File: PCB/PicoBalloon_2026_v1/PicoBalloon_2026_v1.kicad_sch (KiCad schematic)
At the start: 3 parts, among them U1 ATmega328P-A, U2 RFM95W-868S2, U3 GP-02

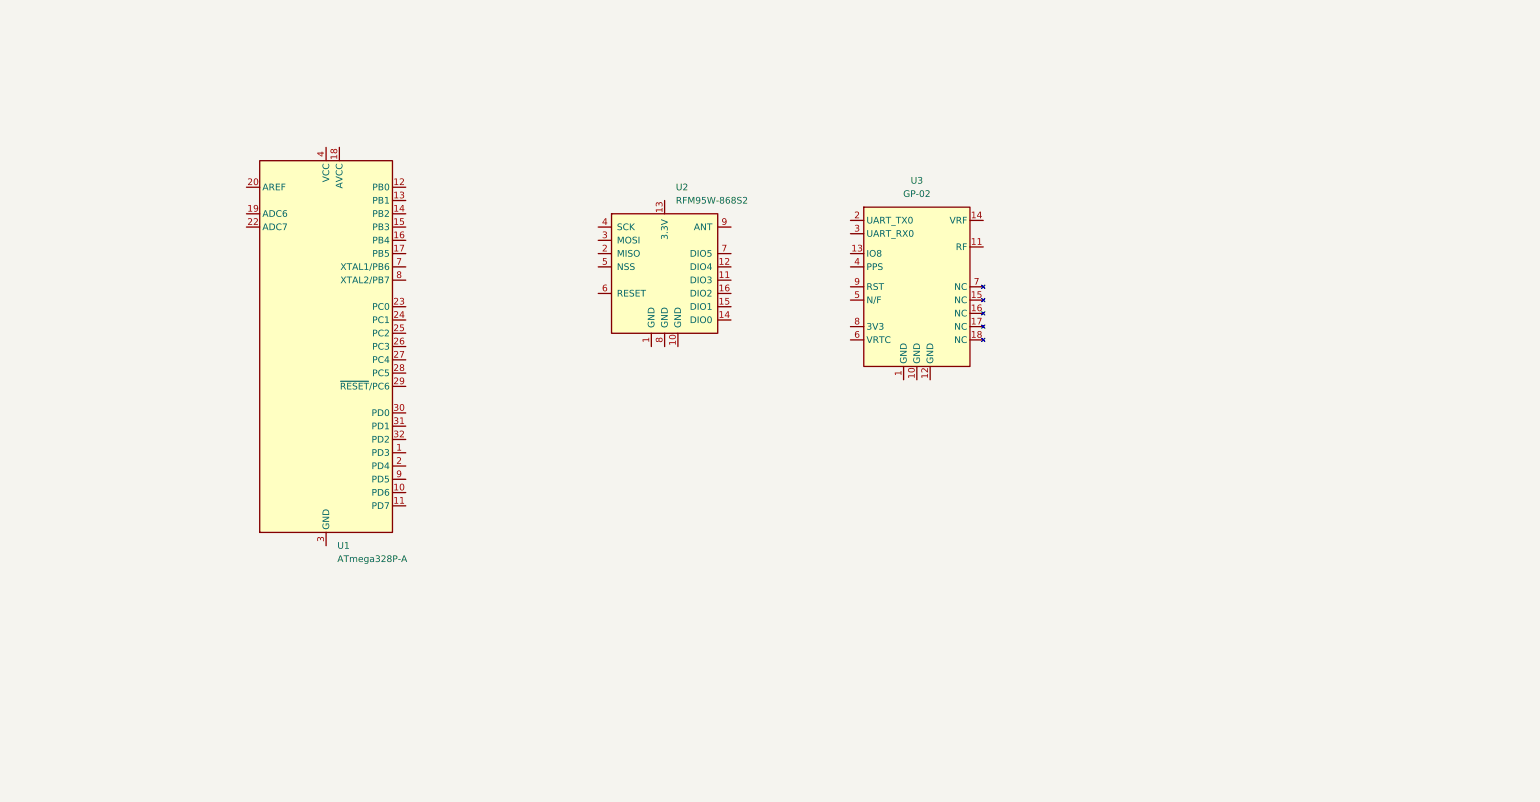
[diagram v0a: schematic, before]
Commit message: [PCB] Schematic update. LoRa power on, GPS power on, VBAT meas. power on.
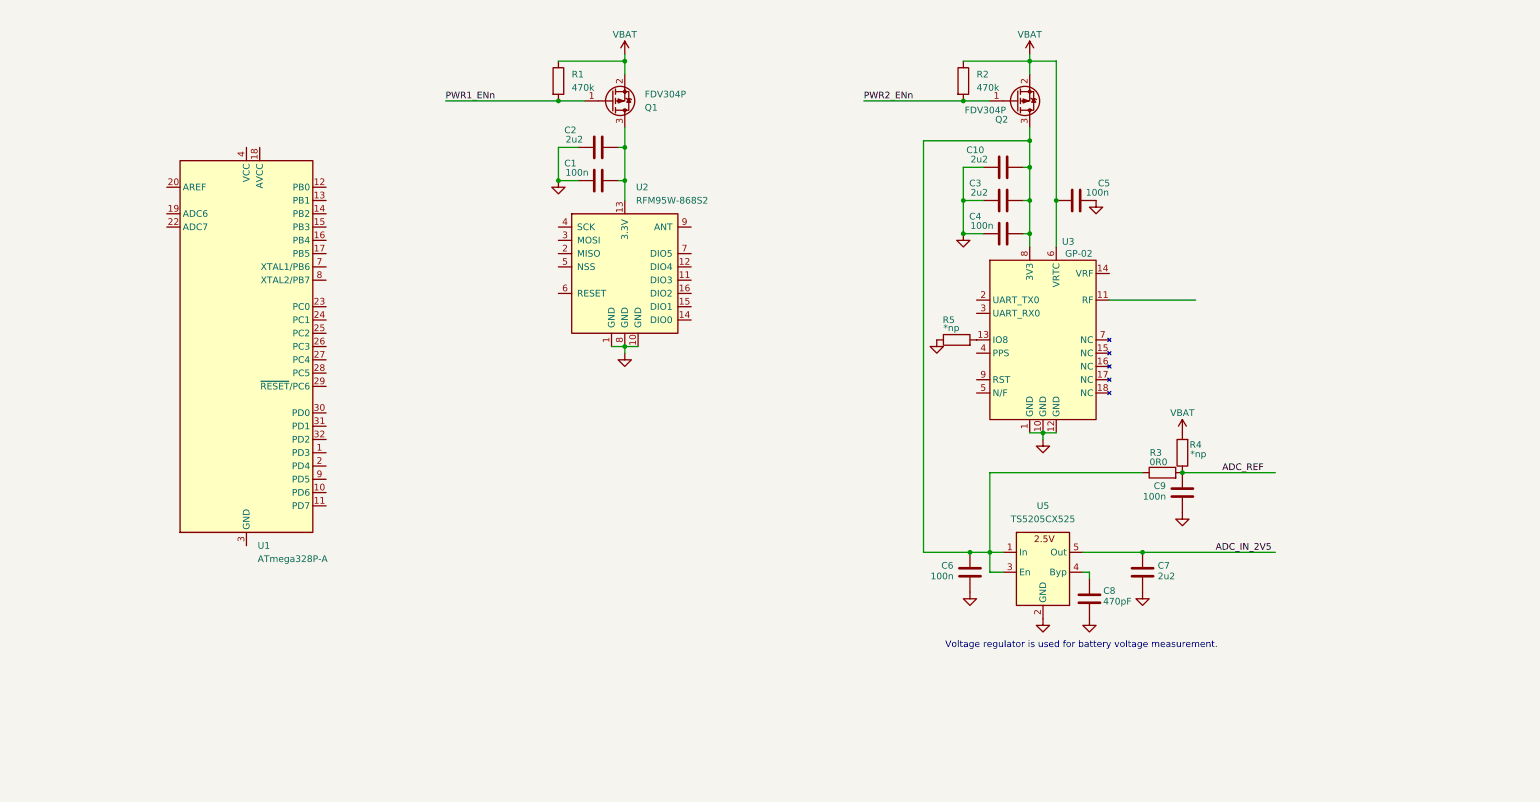
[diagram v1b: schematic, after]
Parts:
- added C1, C4, C5, C6, C9: 100n, Capacitor_SMD:C_0805_2012Metric_Pad1.18x1.45mm_HandSolder, symbol Device:C
- added C10, C2, C3, C7: 2u2, Capacitor_SMD:C_0805_2012Metric_Pad1.18x1.45mm_HandSolder, symbol Device:C
- added C8: 470pF, Capacitor_SMD:C_0805_2012Metric_Pad1.18x1.45mm_HandSolder, symbol Device:C
- added Q1, Q2: FDV304P, Package_TO_SOT_SMD:SOT-23, symbol Jozka_Library:FDV304P
- added R1, R2: 470k, Resistor_SMD:R_0805_2012Metric_Pad1.20x1.40mm_HandSolder, symbol Device:R
- added R3: 0R0, Resistor_SMD:R_0805_2012Metric_Pad1.20x1.40mm_HandSolder, symbol Device:R
- added R4, R5: *np, Resistor_SMD:R_0805_2012Metric_Pad1.20x1.40mm_HandSolder, symbol Device:R
- added U5: TS5205CX525, Package_TO_SOT_SMD:SOT-23-5, symbol Jozka_Library:TS5205
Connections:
- net GND: now reaches U2.1 (GND)
- net GND: now also U2.10 (GND), U2.8 (GND), U3.1 (GND), U3.10 (GND), U3.12 (GND), C1.1, C10.1, C2.1, C3.1, C4.1, C5.1, C6.1, C7.2, C8.1, C9.1, R5.1, U5.2 (GND)
- net at U2.13 (3.3V): now also C1.2, C2.2, Q1.3 (D)
- net at U3.13 (IO8): now also R5.2
- net VBAT: now reaches U3.6 (VRTC)
- net VBAT: now also C5.2, Q1.2 (S), Q2.2 (S), R1.1, R2.1, R4.2
- net at U3.8 (3V3): now also C10.2, C3.2, C4.2, C6.2, Q2.3 (D), R3.1, U5.1 (In), U5.3 (En)
- new net: C8.2, U5.4 (Byp)
- new net ADC_IN_2V5: C7.1, U5.5 (Out)
- new net ADC_REF: C9.2, R3.2, R4.1
- new net PWR1_ENn: Q1.1 (G), R1.2
- new net PWR2_ENn: Q2.1 (G), R2.2
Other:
- note added: "Voltage regulator is used for battery voltage measurement."
- moved on the sheet: U1, U2, U3

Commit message: [PCB] Schematic in progres.
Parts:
- added C11, C12: 22p, Capacitor_SMD:C_0805_2012Metric_Pad1.18x1.45mm_HandSolder, symbol Device:C
- added C13, C16: 2u2, Capacitor_SMD:C_0805_2012Metric_Pad1.18x1.45mm_HandSolder, symbol Device:C
- added C14, C15, C18: 100n, Capacitor_SMD:C_0805_2012Metric_Pad1.18x1.45mm_HandSolder, symbol Device:C
- added J1: Conn_01x07_Pin, Connector_PinHeader_2.54mm:PinHeader_1x07_P2.54mm_Vertical, symbol Connector:Conn_01x07_Pin
- added R10: *np, Resistor_SMD:R_0805_2012Metric_Pad1.20x1.40mm_HandSolder, symbol Device:R
- added R11, R6, R7, R8, R9: 10k, Resistor_SMD:R_0805_2012Metric_Pad1.20x1.40mm_HandSolder, symbol Device:R
- added Y1: 8MHz, Crystal:Crystal_SMD_HC49-SD, symbol Device:Crystal
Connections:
- net ADC_IN_2V5: now also U1.19 (ADC6)
- net ADC_REF: now also U1.20 (AREF)
- net GND: now also U1.21 (GND), U1.3 (GND), U1.5 (GND), C11.2, C12.2, C13.1, C14.1, C15.1, C16.1, C18.1, J1.1 (Pin_1), R11.1
- net PWR1_ENn: now also U1.13 (PB1)
- net VBAT: now also U1.18 (AVCC), U1.4 (VCC), U1.6 (VCC), C13.2, C14.2, C15.2, C16.2, J1.7 (Pin_7), R6.2
- net SPI_MISO: now reaches U2.2 (MISO)
- net SPI_MISO: now also U1.16 (PB4)
- net SPI_MOSI: now reaches U2.3 (MOSI)
- net SPI_MOSI: now also U1.15 (PB3)
- net SPI_SCK: now reaches U2.4 (SCK)
- net SPI_SCK: now also U1.17 (PB5)
- net SPI_SSn: now reaches U2.5 (NSS)
- net SPI_SSn: now also U1.14 (PB2)
- net MCU_RSTn: now reaches U1.29 (~{RESET}/PC6)
- net MCU_RSTn: now also C18.2, J1.2 (Pin_2), R6.1
- net MCU_RX: now reaches U1.30 (PD0)
- net MCU_RX: now also J1.3 (Pin_3), R7.1
- net MCU_TX: now reaches U1.31 (PD1)
- net MCU_TX: now also J1.4 (Pin_4), R9.1
- net at U1.7 (XTAL1/PB6): now also C11.1, Y1.2
- net at U1.8 (XTAL2/PB7): now also C12.1, Y1.1
- net GPS_TX: now reaches U3.2 (UART_TX0)
- net GPS_TX: now also R8.2
- net GPS_RX: now reaches U3.3 (UART_RX0)
- net GPS_RX: now also R10.2, R11.2
- new net GPS_RX_SILENTn: J1.6 (Pin_6), R10.1, R9.2
- new net GPS_TX_SILENTn: J1.5 (Pin_5), R7.2, R8.1
- no-connect marks 0 -> 4
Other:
- note added: "Connect signals GPS_TX_SILENTn and GPS_RX_SILENTn to ground, while the MCU is being programmed."
- note added: "If MCU_TX signal is used as a monitor signal, the R10 wouldn't be placed."
- note added: "Quarterwave transformer 25 Ohm to 50 Ohm at 1575 MHz. The results: A) Microstrip W = 2.62 mm L = 25 mm @ FR4 Er=4.4, H=0.8mm. B) Microstrip W = 1.63 mm L = 25 mm @ FR4 Er=4.4, H=0.5mm."

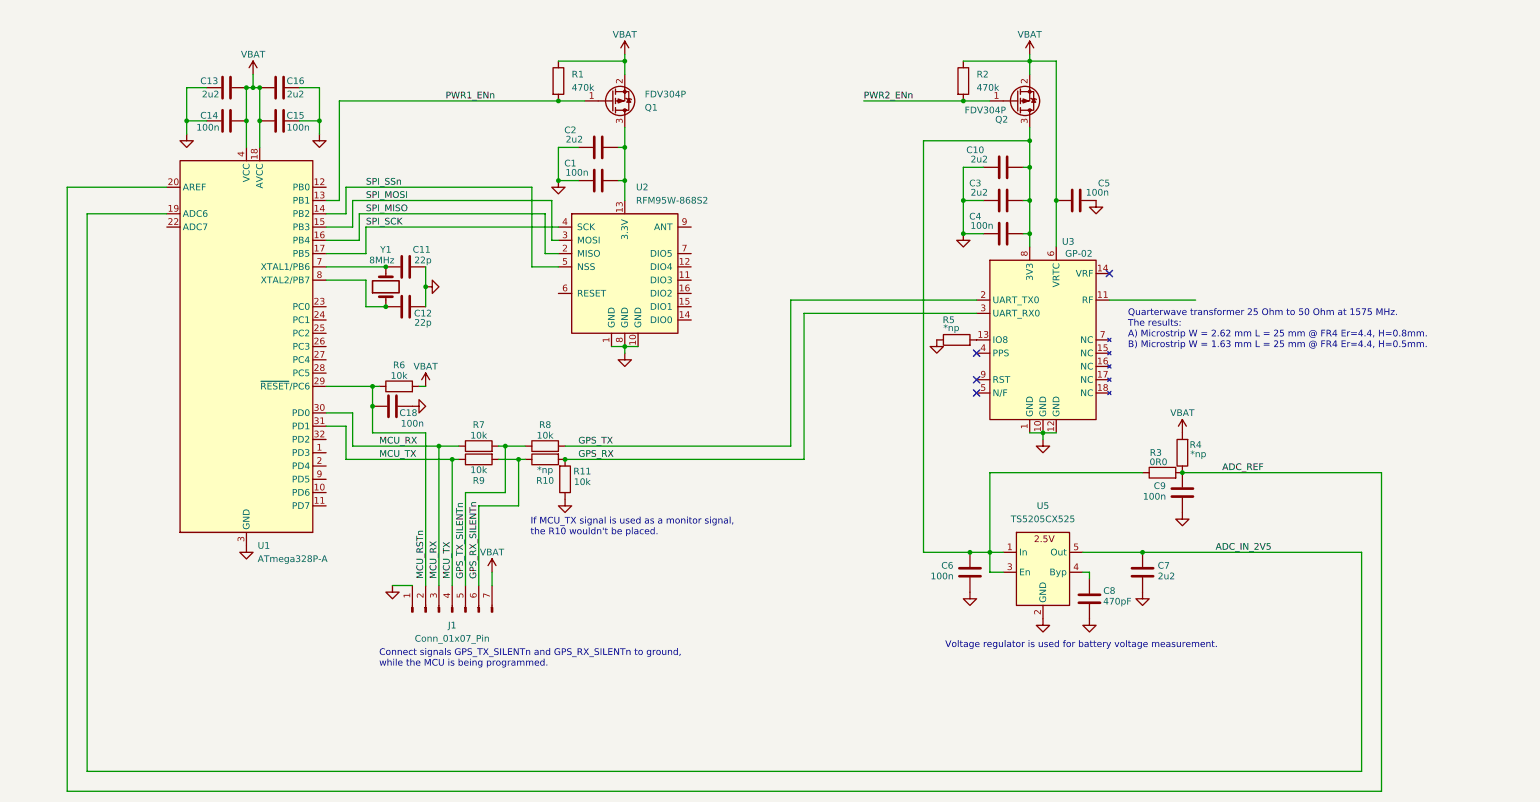
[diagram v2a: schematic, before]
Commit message: [PCB] Schematic drawing update.
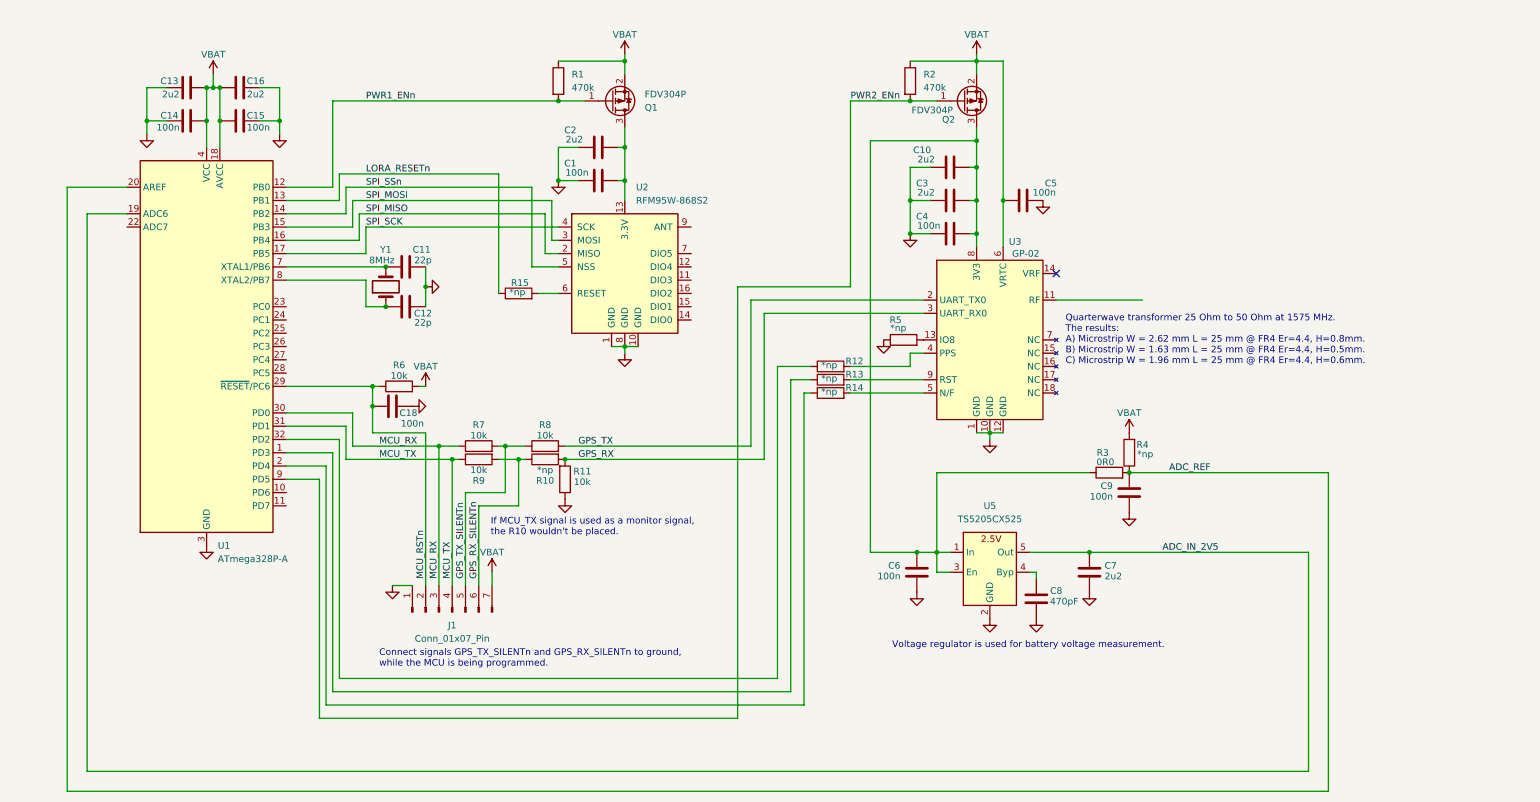
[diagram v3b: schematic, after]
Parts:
- added R12, R13, R14, R15: *np, Resistor_SMD:R_0805_2012Metric_Pad1.20x1.40mm_HandSolder, symbol Device:R
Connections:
- net PWR1_ENn: now also U1.12 (PB0); no longer U1.13 (PB1)
- net PWR2_ENn: now also U1.9 (PD5)
- net at U2.6 (RESET): now also R15.2
- net at U1.1 (PD3): now also R13.1
- net at U1.2 (PD4): now also R14.1
- net at U1.32 (PD2): now also R12.1
- net at U3.4 (PPS): now also R12.2
- net at U3.5 (N/F): now also R14.2
- net at U3.9 (RST): now also R13.2
- new net LORA_RESETn: R15.1, U1.13 (PB1)
- no-connect marks 4 -> 1
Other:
- note added: "Quarterwave transformer 25 Ohm to 50 Ohm at 1575 MHz. The results: A) Microstrip W = 2.62 mm L = 25 mm @ FR4 Er=4.4, H=0.8mm. B) Microstrip W = 1.63 mm L = 25 mm @ FR4 Er=4.4, H=0.5mm. C) Microstrip W = 1.96 mm L = 25 mm @ FR4 Er=4.4, H=0.6mm."
- note removed: "Quarterwave transformer 25 Ohm to 50 Ohm at 1575 MHz. The results: A) Microstrip W = 2.62 mm L = 25 mm @ FR4 Er=4.4, H=0.8mm. B) Microstrip W = 1.63 mm L = 25 mm @ FR4 Er=4.4, H=0.5mm."
- moved on the sheet: C10, C13, C14, C15, C16, C3, C4, C5, C6, C7, C8, C9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

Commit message: [PCB] Antennas drawings added to schematic.
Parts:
- added J10, J8: Conn_01x02_Pin, Connector_PinHeader_1.00mm:PinHeader_1x02_P1.00mm_Vertical, symbol Connector:Conn_01x02_Pin
- added J11: Conn_01x01_Pin, Connector_Wire:SolderWirePad_1x01_SMD_2x4mm, symbol Connector:Conn_01x01_Pin
- added J2, J9: Conn_01x04_Pin, Connector_PinHeader_2.54mm:PinHeader_1x04_P2.54mm_Vertical, symbol Connector:Conn_01x04_Pin
- added J3, J4, J5, J6, J7: Conn_01x02_Pin, Connector_PinHeader_2.54mm:PinHeader_1x02_P2.54mm_Vertical, symbol Connector:Conn_01x02_Pin
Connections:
- net GND: now also J10.1 (Pin_1), J3.2 (Pin_2), J5.1 (Pin_1), J5.2 (Pin_2), J8.1 (Pin_1), J9.1 (Pin_1), J9.2 (Pin_2), J9.3 (Pin_3), J9.4 (Pin_4)
- net VBAT: now also J3.1 (Pin_1)
- net at U2.9 (ANT): now also J8.2 (Pin_2)
- net at U1.23 (PC0): now also J2.4 (Pin_4)
- net at U1.24 (PC1): now also J2.3 (Pin_3)
- net at U1.25 (PC2): now also J2.2 (Pin_2)
- net at U1.26 (PC3): now also J2.1 (Pin_1)
- net at U3.11 (RF): now also J4.1 (Pin_1), J4.2 (Pin_2)
- new net: J6.1 (Pin_1), J6.2 (Pin_2)
- new net: J10.2 (Pin_2), J11.1 (Pin_1)
- new net: J7.1 (Pin_1), J7.2 (Pin_2)
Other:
- note added: "Battery holes must be 2,5 cm away."
- note added: "COAX 50 Ohm"
- note added: "COAX 90°"
- note added: "Feed point"
- note added: "GPS Dipole 1"
- note added: "GSP Dipole 2"
- note added: "Offset feed Monopole"
- note added: "Quarterwave reflectors"
- note added: "Quarterwave transformer 35 Ohm (25 Ohm to 50 Ohm) at 1575 MHz. L = 25 mm @ FR4 Er=4.4, Options: A) Microstrip W = 2.62 mm, H=0.8mm. B) Microstrip W = 1.63 mm, H=0.5mm. C) Microstrip W = 1.96 mm, H=0.6mm."
- note added: "Radiator"
- note added: "TRL 35 Ohm 90°"
- note added: "Two Crossed Dipoles"
- note removed: "Quarterwave transformer 25 Ohm to 50 Ohm at 1575 MHz. The results: A) Microstrip W = 2.62 mm L = 25 mm @ FR4 Er=4.4, H=0.8mm. B) Microstrip W = 1.63 mm L = 25 mm @ FR4 Er=4.4, H=0.5mm. C) Microstrip W = 1.96 mm L = 25 mm @ FR4 Er=4.4, H=0.6mm."
- moved on the sheet: C10, C3, C4, C5, C6, C7, C8, C9, Q2, R12, R13, R14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
